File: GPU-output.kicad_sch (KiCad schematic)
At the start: 26 parts, among them J1 Conn_1-2212115-4, Q1 BSS138PW, Q2 SI7613DN-T1-GE3, Q3 SI7613DN-T1-GE3, U33 SN74LV1T125DBVR, U4 TMCS1100A2-Q1

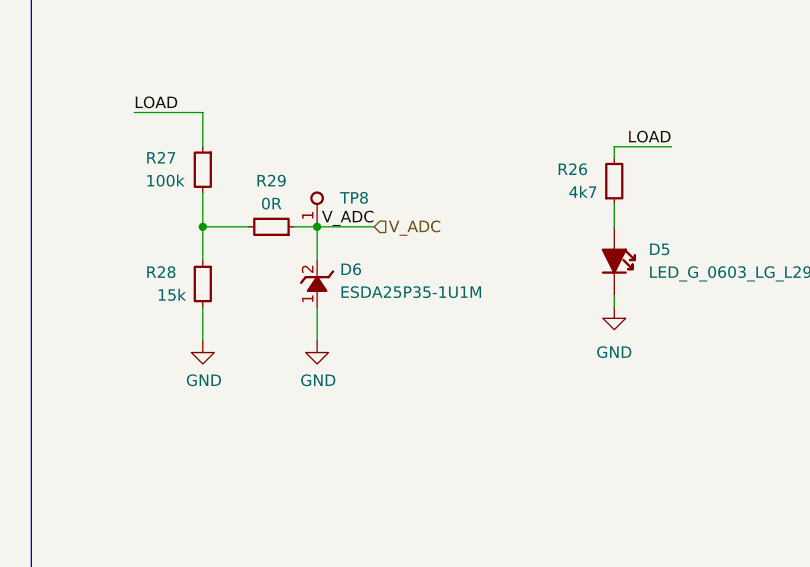
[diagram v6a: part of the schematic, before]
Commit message: Replace tvs diodes on layout
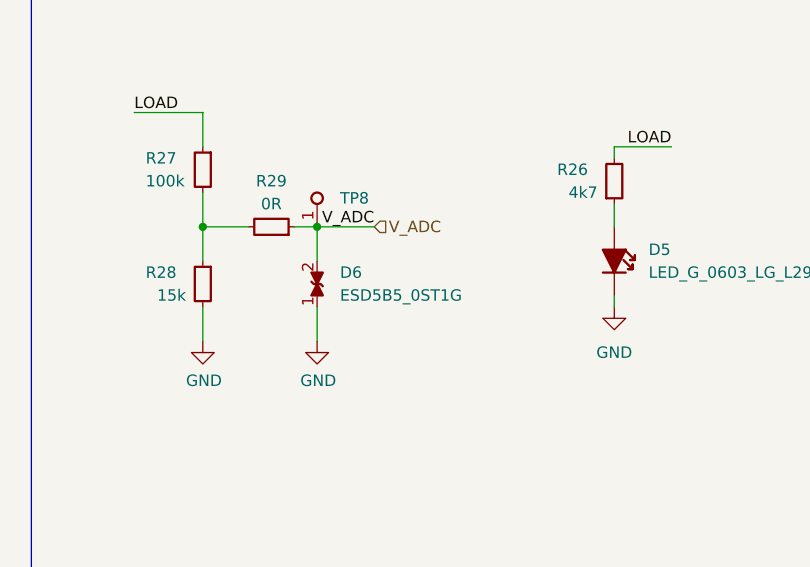
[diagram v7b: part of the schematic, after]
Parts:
- removed D6: ESDA25P35-1U1M, antmicro-footprints:ESDA25P35-1U1M, symbol antmicroTVSDiodes:ESDA25P35-1U1M
- added D6: ESD5B5_0ST1G, antmicro-footprints:SOD-523_NP, symbol antmicroTVSDiodes:ESD5B5_0ST1G
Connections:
- net GND: now also D6.1
- net V_ADC: now also D6.2
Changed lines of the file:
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@@
     (pin "1")
-  )
-  (symbol (lib_id "antmicroTVSDiodes:ESDA25P35-1U1M") (at 193.04 152.4 90) (unit 1)
-    (in_bom yes) (on_board yes) (fields_autoplaced)
-    (property "Reference" "D6" (id 0) (at 195.58 148.2724 90)
-      (effects (font (size 1.27 1.27) (thickness 0.15)) (justify right))
-    )
-    (property "Value" "ESDA25P35-1U1M" (id 1) (at 195.58 150.8124 90)
-      (effects (font (size 1.27 1.27) (thickness 0.15)) (justify right))
-    )
-    (property "Footprint" "antmicro-footprints:ESDA25P35-1U1M" (id 2) (at 203.2 128.27 0)
-      (effects (font (size 1.27 1.27) (thickness 0.15)) (justify left bottom) hide)
-    )
-    (property "Datasheet" "https://www.st.com/resource/en/datasheet/esda25p35-1u1m.pdf" (id 3) (at 205.74 128.27 0)
-      (effects (font (size 1.27 1.27) (thickness 0.15)) (justify left bottom) hide)
-    )
-    (property "MPN" "ESDA25P35-1U1M" (id 4) (at 208.28 128.27 0)
-      (effects (font (size 1.27 1.27) (thickness 0.15)) (justify left bottom) hide)
-    )
-    (property "Manufacturer" "STMicroelectronics" (id 5) (at 210.82 128.27 0)
-      (effects (font (size 1.27 1.27) (thickness 0.15)) (justify left bottom) hide)
-    )
-    (property "Author" "Antmicro" (id 6) (at 213.36 128.27 0)
-      (effects (font (size 1.27 1.27) (thickness 0.15)) (justify left bottom) hide)
-    )
-    (property "License" "Apache-2.0" (id 7) (at 215.9 128.27 0)
-      (effects (font (size 1.27 1.27) (thickness 0.15)) (justify left bottom) hide)
-    )
-    (pin "1")
-    (pin "2")
   )
   (symbol (lib_id "antmicroResistors0402:R_15k_0.1%_0402") (at 180.34 147.32 270) (unit 1)
@@
     (pin "1")
   )
+  (symbol (lib_id "antmicroTVSDiodes:ESD5B5_0ST1G") (at 193.04 152.4 90) (unit 1)
+    (in_bom yes) (on_board yes) (fields_autoplaced)
+    (property "Reference" "D6" (id 0) (at 195.58 148.5899 90)
+      (effects (font (size 1.27 1.27) (thickness 0.15)) (justify right))
+    )
+    (property "Value" "ESD5B5_0ST1G" (id 1) (at 195.58 151.1299 90)
+      (effects (font (size 1.27 1.27) (thickness 0.15)) (justify right))
+    )
+    (property "Footprint" "antmicro-footprints:SOD-523_NP" (id 2) (at 203.2 127 0)
+      (effects (font (size 1.27 1.27) (thickness 0.15)) (justify left bottom) hide)
+    )
+    (property "Datasheet" "https://www.mouser.com/datasheet/2/308/ESD5B5_0ST1_D-1805066.pdf" (id 3) (at 205.74 127 0)
+      (effects (font (size 1.27 1.27) (thickness 0.15)) (justify left bottom) hide)
+    )
+    (property "Manufacturer" "ON Semiconductor" (id 4) (at 208.28 127 0)
+      (effects (font (size 1.27 1.27) (thickness 0.15)) (justify left bottom) hide)
+    )
+    (property "MPN" "ESD5B5.0ST1G" (id 5) (at 210.82 127 0)
+      (effects (font (size 1.27 1.27) (thickness 0.15)) (justify left bottom) hide)
+    )
+    (property "Author" "Antmicro" (id 6) (at 213.36 127 0)
+      (effects (font (size 1.27 1.27) (thickness 0.15)) (justify left bottom) hide)
+    )
+    (property "License" "Apache-2.0" (id 7) (at 215.9 127 0)
+      (effects (font (size 1.27 1.27) (thickness 0.15)) (justify left bottom) hide)
+    )
+    (pin "1")
+    (pin "2")
+  )
   (symbol (lib_id "antmicropower:GND") (at 180.34 156.21 0) (unit 1)
